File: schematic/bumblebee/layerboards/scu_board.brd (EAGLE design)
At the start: 85 x 100 mm, 24 parts

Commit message: Платы отправлены на завод
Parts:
- renumbered U$1 to STM32H405
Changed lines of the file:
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@@
 <drawing>
 <settings>
-<setting alwaysvectorfont="yes"/>
+<setting alwaysvectorfont="no"/>
 <setting verticaltext="up"/>
 </settings>
@@
 <attribute name="VALUE" x="74.217" y="9.843" size="1.016" layer="27" ratio="10" rot="R180"/>
 </element>
-<element name="U$1" library="bluepill" package="SCU" value="SCU" x="43.52" y="38.56" smashed="yes">
-<attribute name="NAME" x="28.52" y="25.06" size="1.27" layer="21"/>
+<element name="STM32H405" library="bluepill" package="SCU" value="SCU" x="43.52" y="38.56" smashed="yes">
+<attribute name="NAME" x="30.52" y="15.56" size="1.27" layer="21"/>
 <attribute name="VALUE" x="28.82" y="4.26" size="1.27" layer="27"/>
 </element>
@@
 <signal name="GND">
 <contactref element="U$2" pad="GND"/>
-<contactref element="U$1" pad="GND_2"/>
+<contactref element="STM32H405" pad="GND_2"/>
 <contactref element="TO_CCU" pad="1"/>
 <contactref element="FROM_PCU" pad="5"/>
@@
 <signal name="5V_SCU">
 <contactref element="U$2" pad="UCC"/>
-<contactref element="U$1" pad="VIN"/>
+<contactref element="STM32H405" pad="VIN"/>
 <contactref element="U$3" pad="VIN"/>
 <contactref element="FROM_PCU" pad="1"/>
@@
 </signal>
 <signal name="SCL3">
-<contactref element="U$1" pad="PA8"/>
+<contactref element="STM32H405" pad="PA8"/>
 <wire x1="22.8636" y1="3" x2="6.1364" y2="3" width="0.2" layer="16"/>
 <wire x1="2.5" y1="6.6364" x2="2.5" y2="37.3636" width="0.2" layer="16"/>
@@
 </signal>
 <signal name="SDA3">
-<contactref element="U$1" pad="PC9"/>
+<contactref element="STM32H405" pad="PC9"/>
 <wire x1="23" y1="2.5" x2="6" y2="2.5" width="0.2" layer="16"/>
 <wire x1="6" y1="2.5" x2="2" y2="6.5" width="0.2" layer="16"/>
@@
 </signal>
 <signal name="ADC_OUT_1">
-<contactref element="U$1" pad="PA1"/>
+<contactref element="STM32H405" pad="PA1"/>
 <wire x1="27.5" y1="11.5" x2="31.5" y2="7.5" width="0.2" layer="1"/>
 <wire x1="27.5" y1="28.15" x2="29.02" y2="29.67" width="0.2" layer="1"/>
@@
 </signal>
 <signal name="N$22">
-<contactref element="U$1" pad="SW-DAT"/>
+<contactref element="STM32H405" pad="SW-DAT"/>
 <contactref element="DEBUG" pad="1"/>
 <wire x1="47.33" y1="13.56" x2="41.89" y2="19" width="0.2" layer="16"/>
@@
 <signal name="N$24">
 <contactref element="DEBUG" pad="2"/>
-<contactref element="U$1" pad="SW-CLK"/>
+<contactref element="STM32H405" pad="SW-CLK"/>
 <wire x1="44.79" y1="13.56" x2="39.85" y2="18.5" width="0.2" layer="16"/>
 <wire x1="39.85" y1="18.5" x2="28.3636" y2="18.5" width="0.2" layer="16"/>
@@
 <signal name="N$6">
 <contactref element="U$7" pad="CRX"/>
-<contactref element="U$1" pad="PA11"/>
+<contactref element="STM32H405" pad="PA11"/>
 <wire x1="54.45" y1="53.55" x2="55.35" y2="52.65" width="0.2" layer="1"/>
 <wire x1="55.35" y1="52.65" x2="55.52" y2="52.53" width="0.2" layer="1"/>
@@
 </signal>
 <signal name="N$7">
-<contactref element="U$1" pad="PA12"/>
+<contactref element="STM32H405" pad="PA12"/>
 <contactref element="U$7" pad="CTX"/>
 <wire x1="55.52" y1="49.99" x2="48.01" y2="49.99" width="0.2" layer="16"/>
@@
 </signal>
 <signal name="N$16">
-<contactref element="U$1" pad="+3.3V"/>
+<contactref element="STM32H405" pad="+3.3V"/>
 <contactref element="U$7" pad="3V3"/>
 <wire x1="55.8656875" y1="54.05" x2="56.97" y2="52.9456875" width="0.3" layer="1"/>
@@
 </signal>
 <signal name="SOL_D_2">
-<contactref element="U$1" pad="PC3"/>
+<contactref element="STM32H405" pad="PC3"/>
 <via x="21.5" y="28" extent="1-16" drill="0.5"/>
 <wire x1="21.5" y1="28" x2="24.05" y2="30.55" width="0.2" layer="16"/>
@@
 </signal>
 <signal name="SOL_D_3">
-<contactref element="U$1" pad="PC4"/>
+<contactref element="STM32H405" pad="PC4"/>
 <via x="20.25" y="28" extent="1-16" drill="0.5"/>
 <wire x1="20.25" y1="28" x2="23.25" y2="31" width="0.2" layer="16"/>
@@
 </signal>
 <signal name="SOL_D_4">
-<contactref element="U$1" pad="PC5"/>
+<contactref element="STM32H405" pad="PC5"/>
 <via x="19" y="28" extent="1-16" drill="0.5"/>
 <wire x1="19" y1="28" x2="22.5" y2="31.5" width="0.2" layer="16"/>
@@
 </signal>
 <signal name="3V3">
-<contactref element="U$1" pad="3.3V"/>
+<contactref element="STM32H405" pad="3.3V"/>
 <via x="16.5" y="25.14" extent="1-16" drill="0.5"/>
 <wire x1="16.5" y1="25.14" x2="26.64" y2="25.14" width="0.5" layer="16"/>
@@
 </signal>
 <signal name="ADC_OUT_2">
-<contactref element="U$1" pad="PA3"/>
+<contactref element="STM32H405" pad="PA3"/>
 <wire x1="27.05" y1="11.3136" x2="27.05" y2="30.24" width="0.2" layer="1"/>
 <wire x1="27.05" y1="11.3136" x2="31.3636" y2="7" width="0.2" layer="1"/>
@@
 <signal name="NSS_2">
 <contactref element="U$2" pad="CSB"/>
-<contactref element="U$1" pad="PB12"/>
+<contactref element="STM32H405" pad="PB12"/>
 <wire x1="39.47" y1="29.02" x2="38.47" y2="30.02" width="0.2" layer="1"/>
 <wire x1="38.47" y1="30.02" x2="36.5" y2="30.02" width="0.2" layer="1"/>
@@
 <signal name="MOSI_2">
 <contactref element="U$2" pad="SDA"/>
-<contactref element="U$1" pad="PB15"/>
+<contactref element="STM32H405" pad="PB15"/>
 <wire x1="42.01" y1="29.02" x2="41.48" y2="29.02" width="0.2" layer="1"/>
 <wire x1="41.48" y1="29.02" x2="40" y2="30.5" width="0.2" layer="1"/>
@@
 <signal name="SCK_2">
 <contactref element="U$2" pad="SCL"/>
-<contactref element="U$1" pad="PB13"/>
+<contactref element="STM32H405" pad="PB13"/>
 <wire x1="44.55" y1="29.02" x2="43.804975" y2="29.02" width="0.2" layer="1"/>
 <wire x1="36.02" y1="28.02" x2="36" y2="28" width="0.2" layer="1"/>
@@
 <signal name="MISO_2">
 <contactref element="U$2" pad="SD0"/>
-<contactref element="U$1" pad="PB14"/>
+<contactref element="STM32H405" pad="PB14"/>
 <wire x1="36.93" y1="29.02" x2="35.6164" y2="29.02" width="0.2" layer="1"/>
 <wire x1="32.97" y1="31.6664" x2="32.97" y2="33.191375" width="0.2" layer="1"/>
@@
 </signal>
 <signal name="SCK_3">
-<contactref element="U$1" pad="PC10"/>
+<contactref element="STM32H405" pad="PC10"/>
 <contactref element="U$3" pad="SCL"/>
 <wire x1="43.44" y1="33.71" x2="47.38" y2="37.65" width="0.2" layer="16"/>
@@
 </signal>
 <signal name="MOSI_3">
-<contactref element="U$1" pad="PC12"/>
+<contactref element="STM32H405" pad="PC12"/>
 <contactref element="U$3" pad="SDA"/>
 <wire x1="40.9" y1="33.71" x2="45.29" y2="38.1" width="0.2" layer="16"/>
@@
 </signal>
 <signal name="MISO_3">
-<contactref element="U$1" pad="PC11"/>
+<contactref element="STM32H405" pad="PC11"/>
 <contactref element="U$3" pad="SAD"/>
 <wire x1="55.52" y1="42.37" x2="52.15" y2="39" width="0.2" layer="16"/>
@@
 </signal>
 <signal name="NSS_3">
-<contactref element="U$1" pad="PD2"/>
+<contactref element="STM32H405" pad="PD2"/>
 <contactref element="U$3" pad="CS"/>
 <wire x1="38.36" y1="33.71" x2="43.2" y2="38.55" width="0.2" layer="16"/>
@@
 <wire x1="81.675" y1="34.175" x2="81.675" y2="90.1886" width="0.2" layer="16"/>
 <wire x1="81.2136" y1="90.65" x2="42.6" y2="90.65" width="0.2" layer="16"/>
-<contactref element="U$1" pad="PA5"/>
+<contactref element="STM32H405" pad="PA5"/>
 <wire x1="58.02" y1="32.21" x2="79.71" y2="32.21" width="0.2" layer="16"/>
 <wire x1="79.71" y1="32.21" x2="81.675" y2="34.175" width="0.2" layer="16"/>
@@
 <wire x1="82.125" y1="33.9886" x2="82.125" y2="90.375" width="0.2" layer="16"/>
 <wire x1="81.4" y1="91.1" x2="47.15" y2="91.1" width="0.2" layer="16"/>
-<contactref element="U$1" pad="PC1"/>
+<contactref element="STM32H405" pad="PC1"/>
 <wire x1="82.125" y1="33.9886" x2="77.8064" y2="29.67" width="0.2" layer="16"/>
 <wire x1="77.8064" y1="29.67" x2="58.02" y2="29.67" width="0.2" layer="16"/>
@@
 <wire x1="81.6" y1="91.55" x2="82.575" y2="90.575" width="0.2" layer="16"/>
 <wire x1="81.6" y1="91.55" x2="53.7" y2="91.55" width="0.2" layer="16"/>
-<contactref element="U$1" pad="PA7"/>
+<contactref element="STM32H405" pad="PA7"/>
 <wire x1="82.575" y1="33.8022" x2="75.9028" y2="27.13" width="0.2" layer="16"/>
 <wire x1="75.9028" y1="27.13" x2="58.02" y2="27.13" width="0.2" layer="16"/>
@@
 <wire x1="82" y1="92" x2="58.25" y2="92" width="0.2" layer="16"/>
 <wire x1="82" y1="92" x2="83.025" y2="90.975" width="0.2" layer="16"/>
-<contactref element="U$1" pad="PB1"/>
+<contactref element="STM32H405" pad="PB1"/>
 <wire x1="71.4592" y1="22.05" x2="58.02" y2="22.05" width="0.2" layer="16"/>
 <wire x1="83.025" y1="90.975" x2="83.025" y2="33.6158" width="0.2" layer="16"/>
@@
 <contactref element="SOL_D_1_2" pad="1"/>
 <contactref element="R9" pad="P$2"/>
-<contactref element="U$1" pad="PC2"/>
+<contactref element="STM32H405" pad="PC2"/>
 <via x="28.5" y="17" extent="1-16" drill="0.5"/>
 <wire x1="28.5" y1="17" x2="29.02" y2="17.52" width="0.2" layer="1"/>

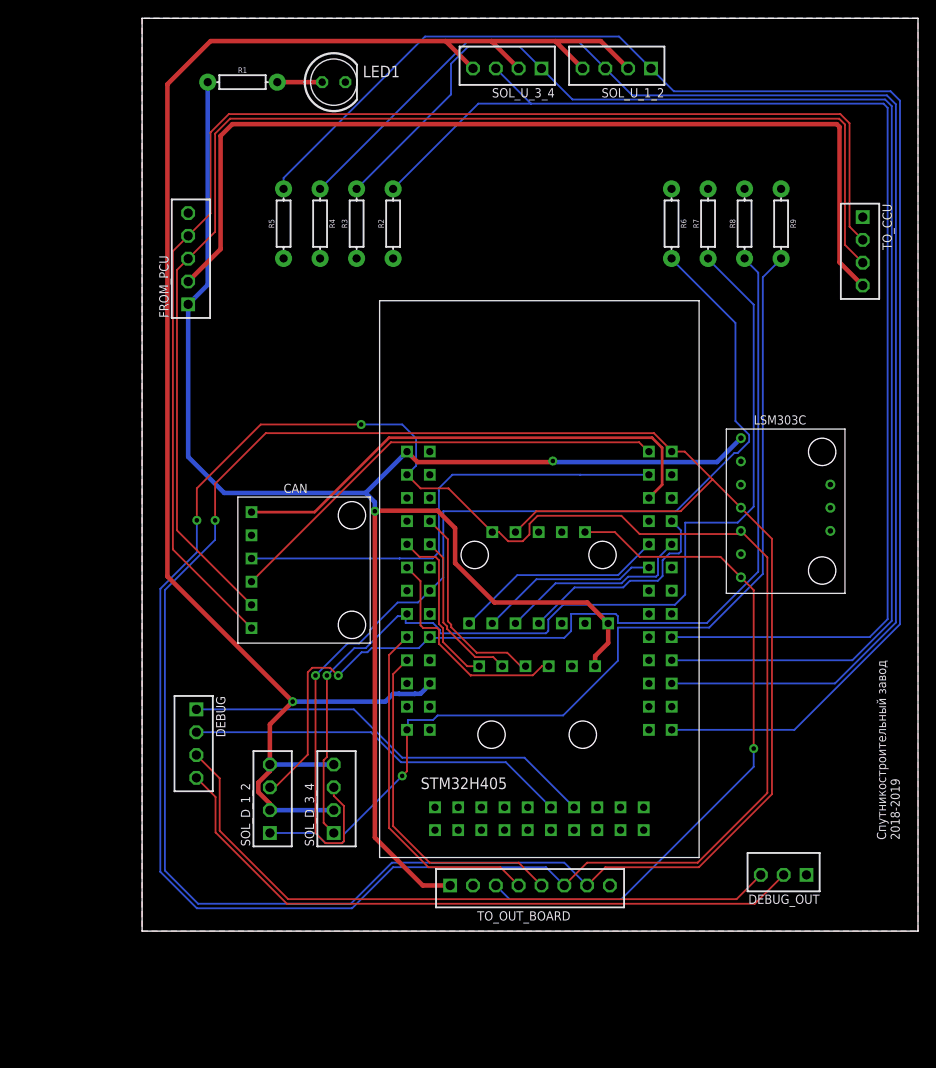
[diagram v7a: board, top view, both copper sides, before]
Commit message: Исправил библиотеку Осталось исправить внешнюю плату и сделать плату под антенну GPS
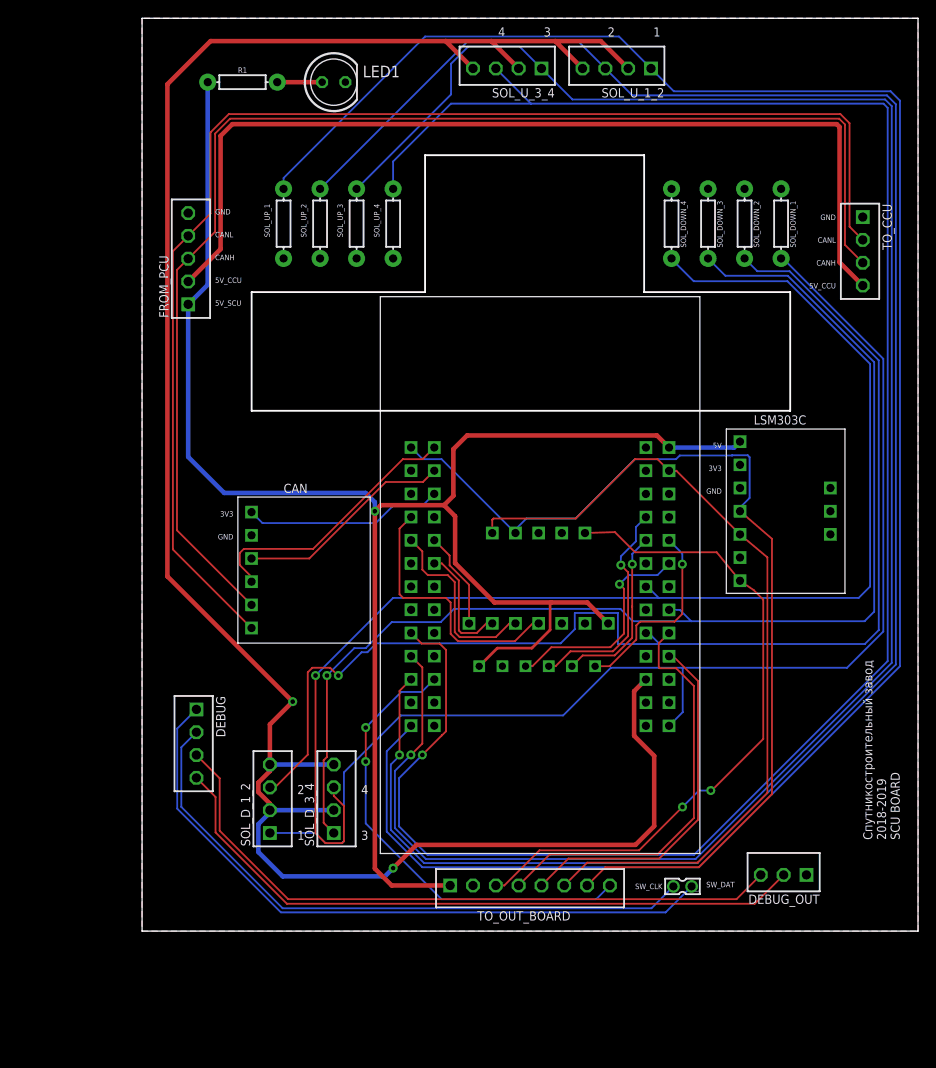
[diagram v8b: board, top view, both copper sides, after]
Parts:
- removed STM32H405: SCU, bluepill:SCU
- added U$1: SCU, bluepill:SCU
- added X1: 332-02, con-garry:332-02
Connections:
- removed net N$22: DEBUG.1, STM32H405.SW-DAT
- removed net N$24: DEBUG.2, STM32H405.SW-CLK
- new net DQ_TEMP: TO_OUT_BOARD.8, U$1.PB0
- new net SW_CLK: DEBUG.2, X1.2
- new net SW_DAT: DEBUG.1, X1.1
- net 3V3: now also U$1.3.3V; no longer STM32H405.3.3V
- net 5V_SCU: now also U$1.VIN, U$2.VCC; no longer STM32H405.VIN, U$2.UCC
- net ADC_OUT_1: now also U$1.PA1; no longer STM32H405.PA1
- net ADC_OUT_2: now also U$1.PA3; no longer STM32H405.PA3
- net GND: now also U$1.GND_2; no longer STM32H405.GND_2
- net MISO_2: now also U$1.PB14, U$2.SDO; no longer STM32H405.PB14, U$2.SD0
- net MISO_3: now also U$1.PC11; no longer STM32H405.PC11
- net MOSI_2: now also U$1.PB15; no longer STM32H405.PB15
- net MOSI_3: now also U$1.PC12; no longer STM32H405.PC12
- net N$16: now also U$1.+3.3V; no longer STM32H405.+3.3V
- net N$6: now also U$1.PA11; no longer STM32H405.PA11
- net N$7: now also U$1.PA12; no longer STM32H405.PA12
- net NSS_2: now also U$1.PB12; no longer STM32H405.PB12
- net NSS_3: now also U$1.PD2; no longer STM32H405.PD2
- net SCK_2: now also U$1.PB13; no longer STM32H405.PB13
- net SCK_3: now also U$1.PC10; no longer STM32H405.PC10
- net SCL3: now also U$1.PA8; no longer STM32H405.PA8
- net SDA3: now also U$1.PC9; no longer STM32H405.PC9
- net SOL_D_1: now also U$1.PC2; no longer STM32H405.PC2
- net SOL_D_2: now also U$1.PC3; no longer STM32H405.PC3
- net SOL_D_3: now also U$1.PC4; no longer STM32H405.PC4
- net SOL_D_4: now also U$1.PC5; no longer STM32H405.PC5
- net SOL_U_1: now also U$1.PB1; no longer STM32H405.PB1
- net SOL_U_2: now also U$1.PA7; no longer STM32H405.PA7
- net SOL_U_3: now also U$1.PC1; no longer STM32H405.PC1
- net SOL_U_4: now also U$1.PA5; no longer STM32H405.PA5
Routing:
- net SDA3: track 223.0 -> 91.2 mm, vias 2 -> 0
- net SCL3: track 239.8 -> 108.2 mm, vias 1 -> 0
- net SW_DAT: track 0.00 -> 74.0 mm
- net SOL_U_4: track 144.2 -> 215.7 mm, vias 0 -> 1
- net SW_CLK: track 0.00 -> 68.4 mm
- net SOL_U_3: track 152.0 -> 216.0 mm, vias 0 -> 1
- net SOL_U_2: track 156.7 -> 217.3 mm, vias 0 -> 1
- net SOL_U_1: track 165.2 -> 219.7 mm
- net 3V3: track 183.6 -> 237.1 mm, vias 1 -> 2
- net DQ_TEMP: track 0.00 -> 51.0 mm, vias 0 -> 2
- net N$22: track 45.8 -> 0.00 mm
- net N$24: track 42.2 -> 0.00 mm
- net N$16: track 54.9 -> 21.8 mm
- net SOL_D_4: track 113.4 -> 145.0 mm
- net SOL_D_2: track 106.6 -> 136.6 mm
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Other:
- outline, holes or cut-outs redrawn
- board text added: "1"
- board text added: "2"
- board text added: "3"
- board text added: "3V3"
- board text added: "4"
- board text added: "5V"
- board text added: "5V_CCU"
- board text added: "5V_SCU"
- board text added: "CANH"
- board text added: "CANL"
- board text added: "GND"
- board text added: "SOL_DOWN_1"
- board text added: "SOL_DOWN_2"
- board text added: "SOL_DOWN_3"
- board text added: "SOL_DOWN_4"
- board text added: "SOL_UP_1"
- board text added: "SOL_UP_2"
- board text added: "SOL_UP_3"
- board text added: "SOL_UP_4"
- board text added: "SW_CLK"
- board text added: "SW_DAT"
- board text added: "Спутникостроительный завод 2018-2019 SCU BOARD"
- board text removed: "Спутникостроительный завод 2018-2019"
